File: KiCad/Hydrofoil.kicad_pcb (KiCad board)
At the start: 2 copper layers, 218 x 35 mm, 19 parts, among them J1 Conn_01x05_Pin, U1 LM334M, U2 LM334M, U3 ADS1115IDGS

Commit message: Start routing on the PCB
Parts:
- moved R6 22.7 mm to (241.1, 107.3)
- moved JP1 20.1 mm to (232.2, 100.3)
- moved C2 12.9 mm to (232.2, 111.1)
- moved R4 10.1 mm to (223.3, 107.3), turned to 0 degrees
- moved R3 9.77 mm to (223.3, 103.5), turned to 180 degrees
- moved R2 9.26 mm to (217.7, 117.5), turned to -90 degrees
- moved U2 7.62 mm to (226.6, 118.1)
- moved U3 6.07 mm to (232.2, 105.4)
- moved R5 3.40 mm to (241.1, 103.5), turned to 180 degrees
- moved L2 2.73 mm to (241.4, 111.1)
- moved L1 2.42 mm to (241.4, 99.7)
- moved U1 2.27 mm to (226.7, 94.0)
- moved C1 1.78 mm to (247.8, 99.7)
- moved R1 1.61 mm to (217.8, 93.3), turned to -90 degrees
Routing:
- net GND: track 103.5 -> 196.4 mm, vias 0 -> 3
- net +5V: track 0.00 -> 86.9 mm
- net AIN0: track 0.00 -> 36.8 mm, vias 0 -> 2
- net AIN1: track 103.5 -> 137.8 mm, vias 0 -> 2
- net Net-(J1-Pin_5): track 0.00 -> 24.4 mm
- net Net-(J1-Pin_1): track 0.00 -> 14.3 mm
- net Net-(JP1-C): track 0.00 -> 10.5 mm
- net SCL: track 0.00 -> 9.92 mm, vias 0 -> 2
- net Net-(R2-Pad1): track 0.00 -> 6.64 mm
- net RDY: track 0.00 -> 6.19 mm
- net Net-(R1-Pad1): track 3.59 -> 6.53 mm

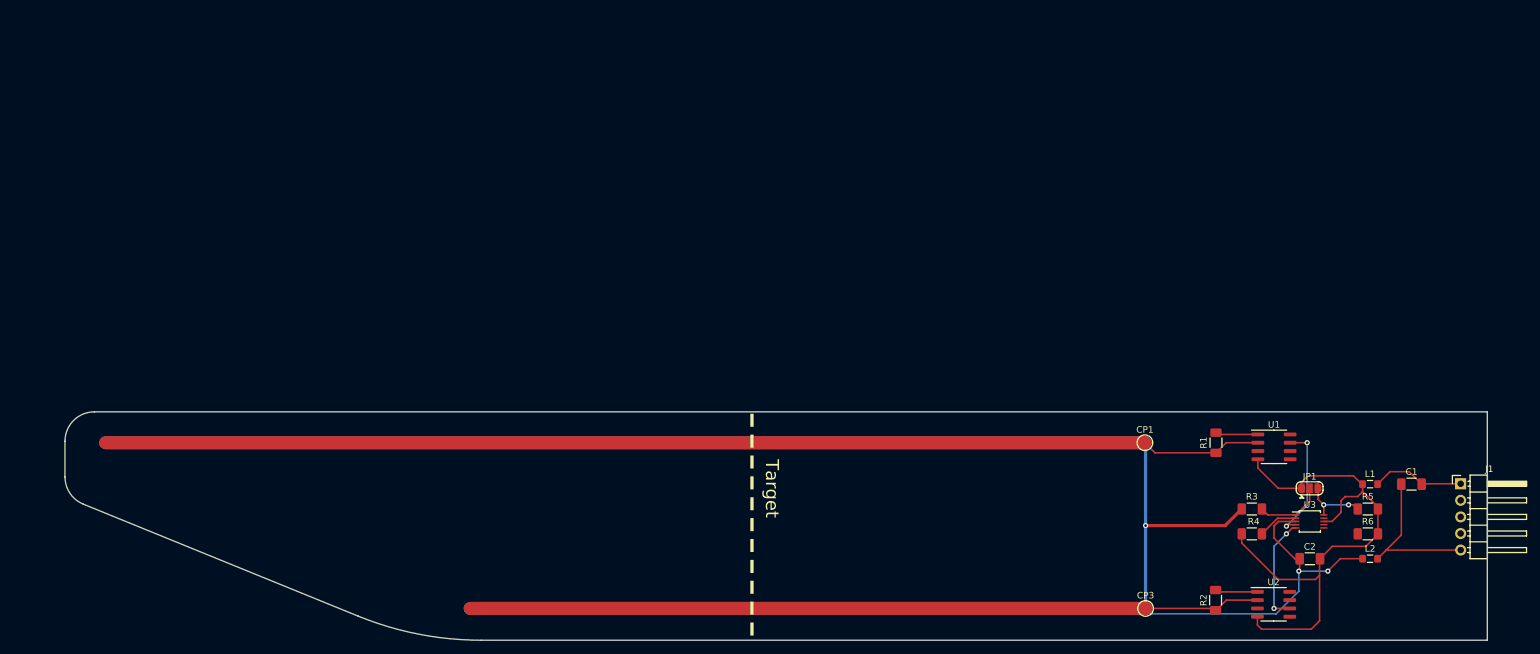
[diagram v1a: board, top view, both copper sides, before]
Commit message: Finalize edgecut, device arrangement, wiring
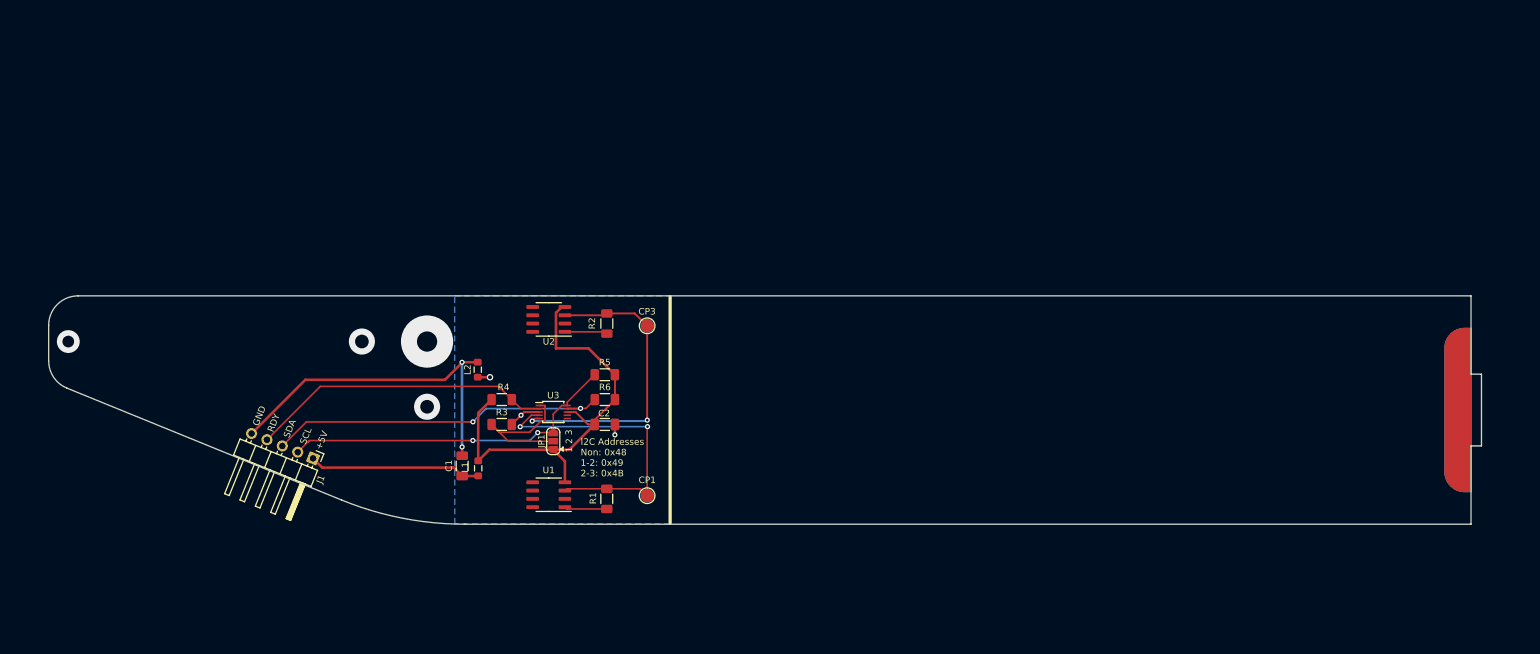
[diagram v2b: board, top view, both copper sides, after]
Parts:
- moved J1 175.9 mm to (79.4, 95.7), turned to -112 degrees
- moved C1 145.5 mm to (102.3, 96.9), turned to 90 degrees
- moved L2 139.8 mm to (104.7, 82.1), turned to 90 degrees
- moved L1 136.7 mm to (104.7, 97.3), turned to -90 degrees
- moved U2 119.4 mm to (115.6, 74.4), turned to 180 degrees
- moved R5 118.7 mm to (124.1, 82.9)
- moved R6 118.7 mm to (124.1, 86.7)
- moved U3 117.2 mm to (116.2, 88.6)
- moved R4 116.8 mm to (108.3, 86.7)
- moved JP1 116.2 mm to (116.2, 93.1), turned to 90 degrees
- moved R3 115.7 mm to (108.3, 90.5), turned to 0 degrees
- moved U1 111.4 mm to (115.5, 101.3), turned to 180 degrees
- moved C2 110.0 mm to (124.1, 90.5), turned to 180 degrees
- moved R2 102.5 mm to (124.4, 75.1), turned to 90 degrees
- moved R1 93.8 mm to (124.4, 102.0), turned to 90 degrees
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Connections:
- net Net-(J1-Pin_1) renamed /+5Vraw
- net Net-(J1-Pin_5) renamed /GNDraw
- net Net-(JP1-C) renamed /ADDR
- net Net-(R1-Pad1) renamed /SETcur1
- net Net-(R2-Pad1) renamed /SETcur2
- J1 pad 2: SDA -> SCL
- J1 pad 3: SCL -> SDA
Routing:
- net GND: track 196.4 -> 8.47 mm
- net AIN1: track 137.8 -> 46.9 mm
- net SDA: track 0.00 -> 52.9 mm, vias 0 -> 2
- net SCL: track 9.92 -> 52.4 mm
- net RDY: track 6.19 -> 46.5 mm
- net /GNDraw: track 24.4 -> 54.1 mm, vias 0 -> 2
- net +5V: track 86.9 -> 67.9 mm
- net /ADDR: track 10.5 -> 23.2 mm
- net /+5Vraw: track 14.3 -> 26.4 mm
- net AIN0: track 36.8 -> 47.0 mm
- net (no net): vias 0 -> 4
- added copper zone on B.Cu, net GND
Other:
- board size 218 x 35 mm -> 219.6 x 35 mm
- board text added: "+5V"
- board text added: "1"
- board text added: "2"
- board text added: "3"
- board text added: "GND"
- board text added: "I2C Addresses Non: 0x48 1-2: 0x49 2-3: 0x4B"
- board text added: "RDY"
- board text added: "SCL"
- board text added: "SDA"
- board text removed: "Target"

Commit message: Add probe-traces
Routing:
- net GND: track 8.47 -> 218.3 mm
- net AIN0: track 47.0 -> 164.5 mm
- net AIN1: track 46.9 -> 139.2 mm
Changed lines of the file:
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@@
     )
     (stroke (width 0.2) (type solid)) (fill solid) (layer "B.Cu"))
-  (gr_line (start 134.14295 70.940538) (end 134.14537 105.707808)
+  (gr_line (start 192.423942 105.694823) (end 192.432715 70.956389)
+    (stroke (width 0.3) (type dash)) (layer "F.SilkS"))
+  (gr_line (start 134.149407 70.996765) (end 134.148989 105.663209)
     (stroke (width 0.5) (type default)) (layer "F.SilkS"))
+  (gr_rect (start 135.717278 98.53908) (end 247.795002 102.699637)
+    (stroke (width 0.15) (type solid)) (fill solid) (layer "B.Mask"))
   (gr_poly
     (pts
@@
     )
     (stroke (width 0.2) (type solid)) (fill solid) (layer "B.Mask"))
+  (gr_rect (start 135.786546 73.838201) (end 222.745658 78.064631)
+    (stroke (width 0.15) (type solid)) (fill solid) (layer "B.Mask"))
+  (gr_rect (start 135.719194 98.538856) (end 247.796918 102.699413)
+    (stroke (width 0.15) (type solid)) (fill solid) (layer "F.Mask"))
+  (gr_rect (start 135.797233 73.834101) (end 222.756345 78.060531)
+    (stroke (width 0.15) (type solid)) (fill solid) (layer "F.Mask"))
   (gr_poly
     (pts
@@
   (gr_circle (center 86.895186 77.836465) (end 86.895186 75.836465)
     (stroke (width 0.2) (type solid)) (fill none) (layer "Dwgs.User"))
+  (gr_line (start 222.726434 105.838773) (end 222.739743 70.860171)
+    (stroke (width 0.15) (type default)) (layer "Dwgs.User"))
   (gr_circle (center 41.895186 77.836465) (end 40.995186 77.836465)
     (stroke (width 0.2) (type solid)) (fill none) (layer "Dwgs.User"))
+  (gr_rect (start 135.731525 100.564255) (end 247.787205 102.702173)
+    (stroke (width 0.15) (type default)) (fill none) (layer "Dwgs.User"))
+  (gr_line (start 247.799607 105.778075) (end 247.797188 70.833351)
+    (stroke (width 0.15) (type default)) (layer "Dwgs.User"))
+  (gr_line (start 135.731525 105.752697) (end 135.738785 70.874518)
+    (stroke (width 0.15) (type default)) (layer "Dwgs.User"))
+  (gr_rect (start 135.738785 70.874518) (end 247.76694 73.925042)
+    (stroke (width 0.15) (type default)) (fill none) (layer "Dwgs.User"))
   (gr_circle (center 96.895186 77.836465) (end 95.345186 77.836465)
     (stroke (width 0.2) (type solid)) (fill none) (layer "Dwgs.User"))
+  (gr_rect (start 135.731525 102.702173) (end 247.75968 105.752697)
+    (stroke (width 0.15) (type default)) (fill none) (layer "Dwgs.User"))
   (gr_circle (center 86.895186 77.836465) (end 85.845186 77.836465)
     (stroke (width 0.2) (type solid)) (fill none) (layer "Dwgs.User"))
@@
   (gr_circle (center 96.895186 77.836465) (end 96.895186 73.836465)
     (stroke (width 0.2) (type solid)) (fill none) (layer "Dwgs.User"))
+  (gr_rect (start 135.738785 75.917467) (end 247.79808 78.055385)
+    (stroke (width 0.15) (type default)) (fill none) (layer "Dwgs.User"))
   (gr_line (start 256.895186 105.836465) (end 256.895186 70.836465)
     (stroke (width 0.2) (type solid)) (layer "Dwgs.User"))
+  (gr_rect (start 135.731525 98.57183) (end 247.797004 100.564255)
+    (stroke (width 0.15) (type default)) (fill none) (layer "Dwgs.User"))
   (gr_circle (center 41.895186 77.836465) (end 41.895186 76.086465)
     (stroke (width 0.2) (type solid)) (fill none) (layer "Dwgs.User"))
+  (gr_rect (start 135.738785 73.925042) (end 247.801427 75.917467)
+    (stroke (width 0.15) (type default)) (fill none) (layer "Dwgs.User"))
   (gr_arc (start 38.895186 75.336465) (mid 40.213205 72.154484) (end 43.395186 70.836465)
     (stroke (width 0.2) (type solid)) (layer "Edge.Cuts"))
@@
   (via (at 41.900724 77.840628) (size 3.5) (drill 1.8) (layers "F.Cu" "B.Cu") (net 0))
   (via (at 96.889543 77.839765) (size 8) (drill 3.1) (layers "F.Cu" "B.Cu") (net 0))
+  (segment (start 130.617262 101.461011) (end 134.85506 101.461011) (width 0.25) (layer "F.Cu") (net 1))
   (segment (start 130.617262 101.461011) (end 130.617262 90.943201) (width 0.25) (layer "F.Cu") (net 1))
   (segment (start 112.86691 89.139054) (end 114.080271 89.139054) (width 0.25) (layer "F.Cu") (net 1))
+  (segment (start 134.85506 101.461011) (end 135.765598 100.550473) (width 0.25) (layer "F.Cu") (net 1))
   (segment (start 111.155845 90.850119) (end 112.86691 89.139054) (width 0.25) (layer "F.Cu") (net 1))
   (segment (start 130.617262 90.943201) (end 130.678473 90.88199) (width 0.25) (layer "F.Cu") (net 1))
+  (segment (start 135.765598 100.550473) (end 247.785627 100.550473) (width 2) (layer "F.Cu") (net 1))
   (segment (start 124.431385 100.402747) (end 129.558998 100.402747) (width 0.25) (layer "F.Cu") (net 1))
   (segment (start 118.016385 100.682747) (end 118.296385 100.402747) (width 0.25) (layer "F.Cu") (net 1))
@@
   (via (at 125.678214 92.141734) (size 0.8) (drill 0.4) (layers "F.Cu" "B.Cu") (net 5))
   (via (at 106.532044 83.310462) (size 1) (drill 0.6) (layers "F.Cu" "B.Cu") (free) (net 5))
+  (segment (start 130.617262 101.461011) (end 134.853368 101.461011) (width 0.4) (layer "B.Cu") (net 5))
+  (segment (start 135.248189 75.426011) (end 135.734341 75.912163) (width 0.4) (layer "B.Cu") (net 5))
+  (segment (start 134.853368 101.461011) (end 135.763682 100.550697) (width 0.4) (layer "B.Cu") (net 5))
+  (segment (start 135.763682 100.550697) (end 247.783711 100.550697) (width 2) (layer "B.Cu") (net 5))
+  (segment (start 130.617262 75.426011) (end 135.248189 75.426011) (width 0.4) (layer "B.Cu") (net 5))
+  (segment (start 135.734341 75.912163) (end 222.721049 75.912163) (width 2) (layer "B.Cu") (net 5))
   (segment (start 124.441984 73.531972) (end 128.723223 73.531972) (width 0.3) (layer "F.Cu") (net 6))
+  (segment (start 135.262976 75.426011) (end 135.745028 75.908063) (width 0.3) (layer "F.Cu") (net 6))
   (segment (start 128.723223 73.531972) (end 130.617262 75.426011) (width 0.3) (layer "F.Cu") (net 6))
+  (segment (start 135.745028 75.908063) (end 222.731736 75.908063) (width 2) (layer "F.Cu") (net 6))
   (segment (start 124.161984 73.811972) (end 124.441984 73.531972) (width 0.3) (layer "F.Cu") (net 6))
   (segment (start 113.006052 90.025217) (end 113.392215 89.639054) (width 0.25) (layer "F.Cu") (net 6))
+  (segment (start 130.617262 75.426011) (end 135.262976 75.426011) (width 0.3) (layer "F.Cu") (net 6))
   (segment (start 130.617262 75.426011) (end 130.617262 89.860093) (width 0.3) (layer "F.Cu") (net 6))
   (segment (start 113.392215 89.639054) (end 114.065422 89.639054) (width 0.25) (layer "F.Cu") (net 6))
   (segment (start 130.617262 89.860093) (end 130.640383 89.883214) (width 0.3) (layer "F.Cu") (net 6))
   (segment (start 118.026984 73.811972) (end 124.161984 73.811972) (width 0.3) (layer "F.Cu") (net 6))
+  (segment (start 135.744155 75.908936) (end 135.745028 75.908063) (width 0.25) (layer "F.Cu") (net 6))
   (via (at 130.640383 89.883214) (size 0.8) (drill 0.4) (layers "F.Cu" "B.Cu") (net 6))
   (via (at 113.006052 90.025217) (size 0.8) (drill 0.4) (layers "F.Cu" "B.Cu") (free) (net 6))

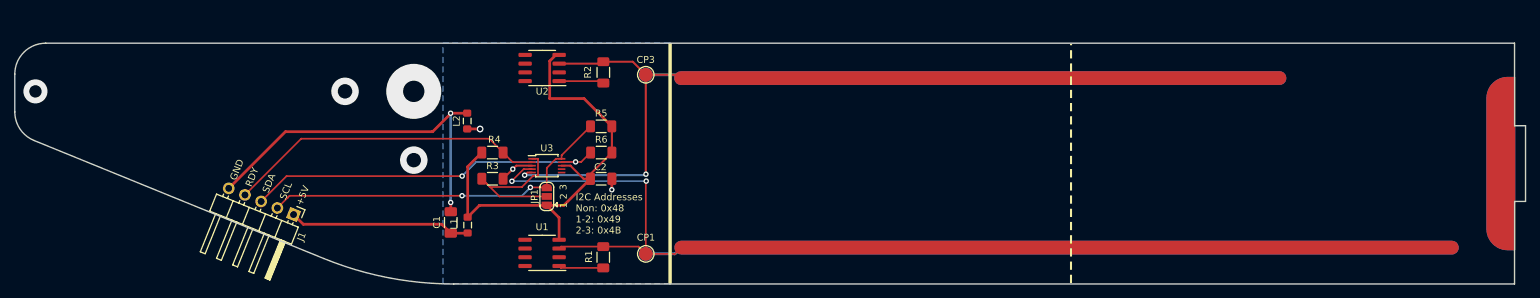
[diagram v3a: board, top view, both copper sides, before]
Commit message: Add PS to the curcuit, change PCB outline
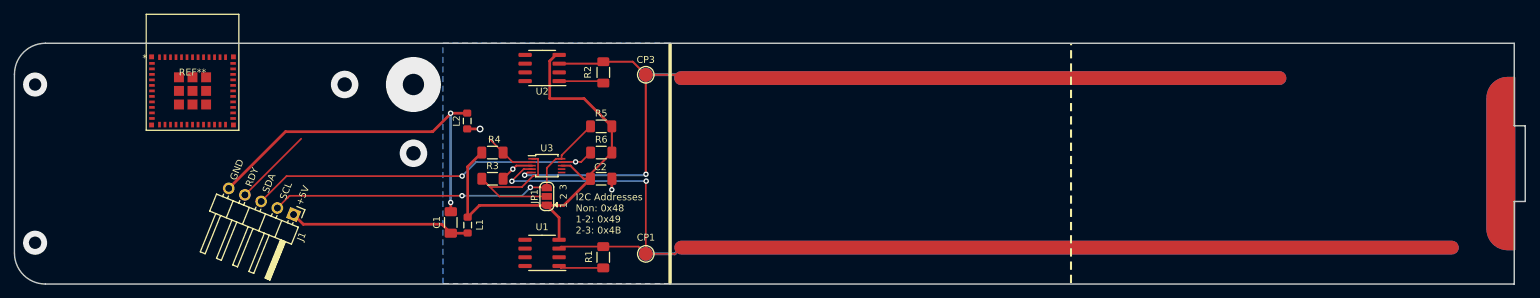
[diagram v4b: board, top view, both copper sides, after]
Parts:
- added REF**: ESP32-C3-MINI-1_EXP, ESP32-C3-MINI-1-N4:ESP32-C3-MINI-1_EXP, F.Cu at (64.7, 75.1)
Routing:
- net RDY: track 46.5 -> 19.2 mm
- net (no net): vias 4 -> 5
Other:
- outline, holes or cut-outs redrawn
